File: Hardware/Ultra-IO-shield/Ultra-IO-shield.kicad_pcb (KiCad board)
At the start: 4 copper layers, 158.3 x 36.7 mm, 89 parts, among them J1 Conn_01x04, J10 ASSMANN_A-DF_09_PP/Z, J11 TC_1578891_SCART, J12 Conn_01x01, J13 Conn_01x02, J14 CUI_SD-50BV, J15 Conn_01x02, J16 CUI_SD-50BV, J17 CUI_SD-50BV, J18 Conn_01x04, J19 Conn_01x04, J2 DIN-8_SD-80BV, J20 Conn_01x02, J21 ASSMANN_A-DF_09_PP/Z, J22 Conn_01x02, J3 Conn_01x04, J4 Conn_01x06, J5 Conn_01x02, J6 Conn_RCJ-023, J7 Conn_RCJ-022, J8 Conn_01x02, J9 NorComp_111-014-213L001, Q1 MMBT2907AM3T5G, U1 LM211, U2 AP7370, U3 ADuM226

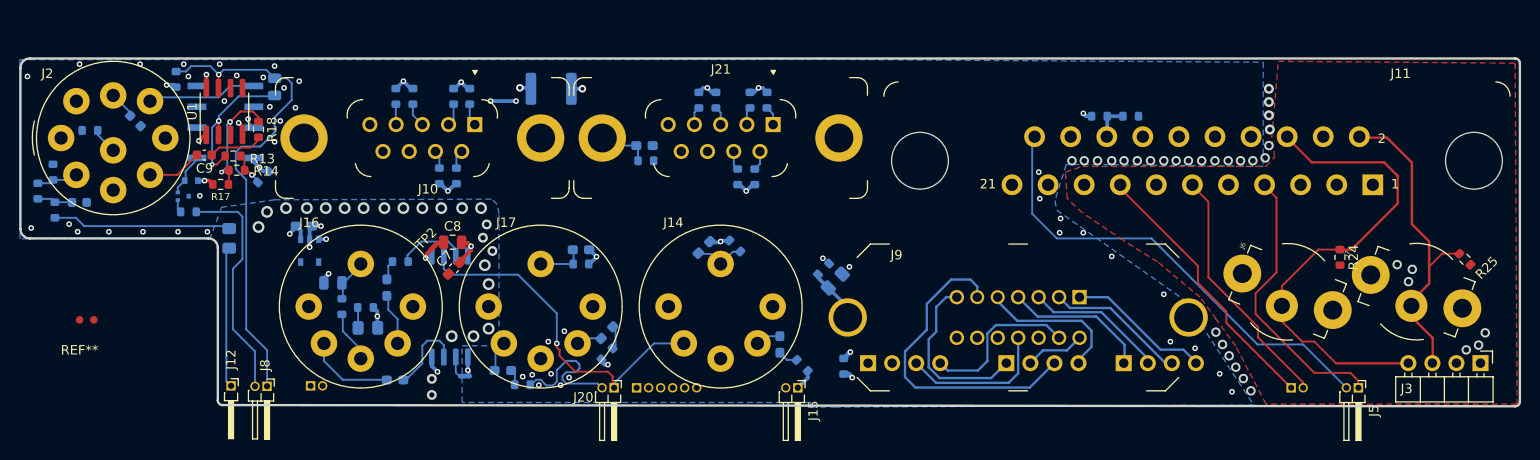
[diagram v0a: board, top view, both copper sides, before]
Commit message: Redesigning of the IO-shield, to make room for Keyboard, power and USB.
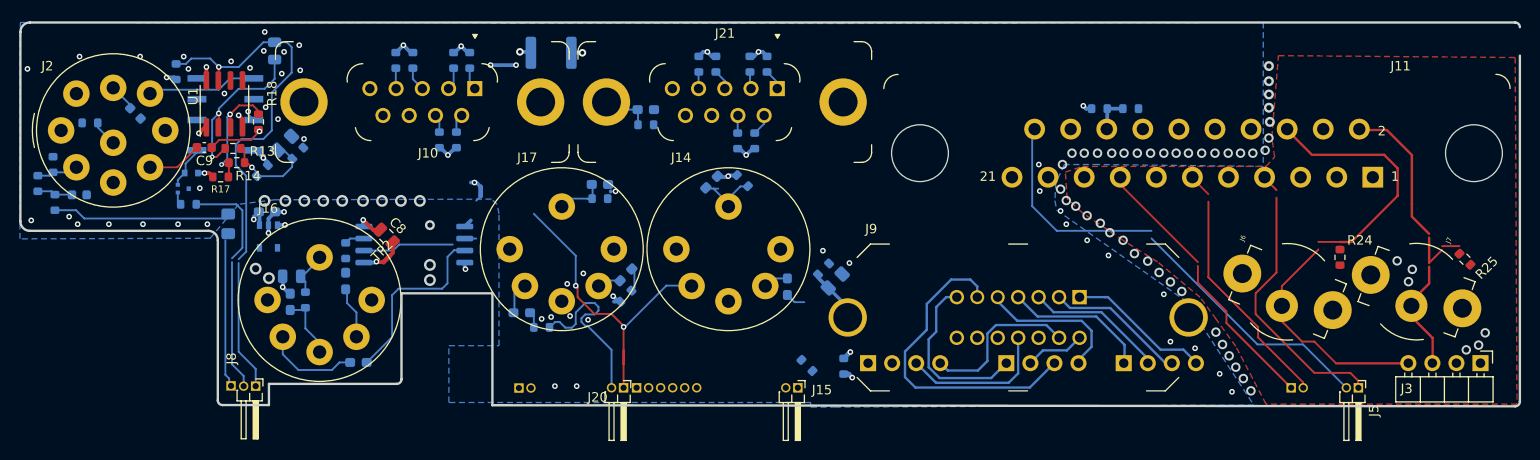
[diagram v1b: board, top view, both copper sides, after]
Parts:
- removed REF**: TestPoint_Bridge_Pitch1.5mm_Pad0.8mm, LRJ:TestPoint_Bridge_Pitch1.5mm_Pad0.8mm
- C7, J12: moved to B.Cu
- moved J13 22.0 mm to (143.0, 109.5)
- moved C2 21.4 mm to (118.3, 83.7), turned to 45 degrees
- moved TP1 19.6 mm to (139.0, 88.8), turned to -90 degrees
- moved R16 17.8 mm to (119.7, 84.7), turned to 45 degrees
- moved C7 17.7 mm to (118.8, 100.4), turned to 90 degrees
- moved U3 7.55 mm to (132.0, 94.3), turned to 0 degrees
- moved C3 7.18 mm to (151.6, 88.0)
- moved R6 7.18 mm to (151.6, 89.5)
- moved C8 7.03 mm to (129.0, 93.5), turned to 135 degrees
- moved C1 6.95 mm to (163.3, 87.8)
- moved R2 6.95 mm to (166.6, 87.6)
- moved J17 6.46 mm to (147.5, 94.8)
- moved FB1 6.42 mm to (154.3, 97.5)
- moved FB5 6.42 mm to (143.3, 101.5)
- moved R5 6.42 mm to (154.3, 99.8)
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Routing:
- net +12V: track 86.8 -> 45.4 mm
- net /CSINKi: track 8.58 -> 19.5 mm
- net /MID_RX: track 37.1 -> 43.6 mm, vias 1 -> 2
- net /CSRCi: track 7.66 -> 2.12 mm
- net Net-(C2-Pad1): track 5.85 -> 10.7 mm
- net GND: track 11.0 -> 6.58 mm
- net /CAS_IN: track 52.0 -> 56.3 mm
- net /MID_TX: track 15.3 -> 19.1 mm
- net +5V: track 27.7 -> 24.2 mm
- net Net-(R12-Pad1): track 15.4 -> 17.9 mm
- net Net-(FB2-Pad2): track 1.88 -> 0.00 mm
- net /+12V-1K: track 74.8 -> 76.7 mm
- net Net-(C7-Pad1): track 5.33 -> 6.99 mm
- net /+5VD_: track 13.9 -> 15.2 mm
- net /CAS_OUT: track 14.9 -> 16.0 mm
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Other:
- board size 158.3 x 36.7 mm -> 158.3 x 40.5 mm

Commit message: Multiple redesigns of the IO-shield. Replaced FPGA with lower pin-count AT10K, since the higher pin-count one is now obsolete.
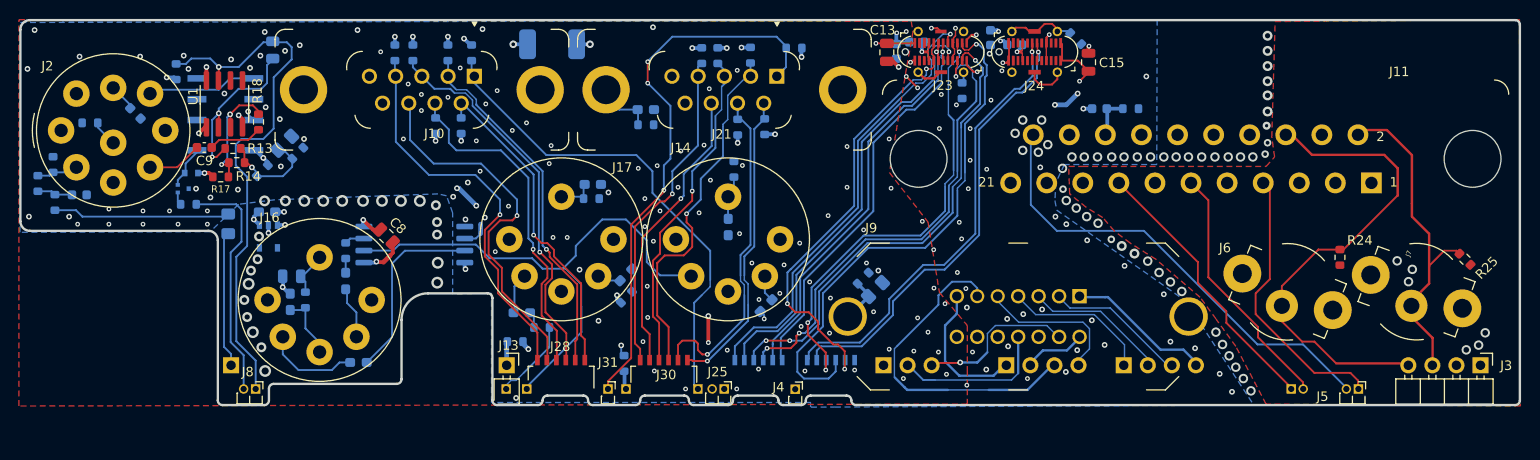
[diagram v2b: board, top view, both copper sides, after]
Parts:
- added C13: C_GRM21BR61A476ME15K, Capacitor_SMD:C_0805_2012Metric, F.Cu at (181.8, 74.0)
- added C14: C_CL10B104KB8NNNL, LRJ:C_0603_1608Metric_round_court, B.Cu at (182.8, 74.0)
- added C15: C_GRM21BR61A476ME15K, Capacitor_SMD:C_0805_2012Metric, F.Cu at (203.2, 75.1)
- added C16: C_CL10B104KB8NNNL, LRJ:C_0603_1608Metric_round_court, B.Cu at (192.8, 72.5)
- added F2: PPTC_0603L075, Fuse:Fuse_0603_1608Metric, B.Cu at (185.0, 73.0)
- added F3: PPTC_0603L075, Fuse:Fuse_0603_1608Metric, B.Cu at (195.3, 73.2)
- added J23: USB_C_GCT_USB4115-03-C, LRJ:USB_C_Receptacle_GCT_USB4115-03-C, F.Cu at (187.6, 74.0)
- added J24: USB_C_GCT_USB4115-03-C, LRJ:USB_C_Receptacle_GCT_USB4115-03-C, F.Cu at (197.5, 74.0)
- added J25: Conn_01x02, LRJ:PinHeader_1x02_P1.27mm_Horizontal_less-silk, F.Cu at (164.7, 109.6)
- added J26: BC075-06, LRJ:GCT_BC075-06_PinHeader_1x06_P1.00mm_Horizontal_SMD, B.Cu at (168.3, 107.3)
- added J27: BC075-06, LRJ:GCT_BC075-06_PinHeader_1x06_P1.00mm_Horizontal_SMD, B.Cu at (175.9, 107.3)
- added J28: BC075-06, LRJ:GCT_BC075-06_PinHeader_1x06_P1.00mm_Horizontal_SMD, F.Cu at (147.4, 107.3)
- added J29: Conn_01x02, LRJ:PinHeader_1x01_P1.27mm_Horizontal_less-silk, B.Cu at (161.9, 109.6)
- added J30: BC075-06, LRJ:GCT_BC075-06_PinHeader_1x06_P1.00mm_Horizontal_SMD, F.Cu at (158.3, 107.3)
- added J31: Conn_01x02, LRJ:PinHeader_1x01_P1.27mm_Horizontal_less-silk, F.Cu at (152.4, 109.6)
- added J32: Conn_01x02, LRJ:PinHeader_1x01_P1.27mm_Horizontal_less-silk, B.Cu at (143.8, 109.6)
- added R39: R_ERJ-3GEYJ105V, Resistor_SMD:R_0603_1608Metric, B.Cu at (189.8, 78.1)
- added R40: R_ERJ-3GEYJ105V, Resistor_SMD:R_0603_1608Metric, B.Cu at (201.8, 72.6)
- C11, C9: value C -> 22nF
- F1: footprint Fuse:Fuse_1812_4532Metric -> LRJ:Yageo_Fuse_1812_4532Metric
- J12: footprint Connector_PinHeader_1.27mm:PinHeader_1x01_P1.27mm_Horizontal -> LRJ:PinHeader_1x01_P2.54mm_Horizontal_less-silk
- J13: value Conn_01x02 -> Conn_01x01; footprint Connector_PinHeader_1.27mm:PinHeader_1x02_P1.27mm_Horizontal -> LRJ:PinHeader_1x01_P2.54mm_Horizontal_less-silk; moved to F.Cu
- J15, J20: footprint Connector_PinHeader_1.27mm:PinHeader_1x02_P1.27mm_Horizontal -> LRJ:PinHeader_1x01_P1.27mm_Horizontal_less-silk; moved to B.Cu
- J19: value Conn_01x04 -> Conn_01x03; footprint LRJ:PinHeader_1x04_P2.54mm_Horizontal_less-silk -> LRJ:PinHeader_1x03_P2.54mm_Horizontal_less-silk
- J22, J5, J8: footprint Connector_PinHeader_1.27mm:PinHeader_1x02_P1.27mm_Horizontal -> LRJ:PinHeader_1x02_P1.27mm_Horizontal_less-silk
- J4: value Conn_01x06 -> Conn_01x02; footprint Connector_PinHeader_1.27mm:PinHeader_1x06_P1.27mm_Horizontal -> LRJ:PinHeader_1x01_P1.27mm_Horizontal_less-silk; moved to F.Cu
- R11, R23: value R -> 1K
- R12: value R -> 220K; footprint Resistor_SMD:R_0805_2012Metric -> LRJ:R_0805_2012Metric_roundcourt
- R13, R21, R22: value R -> 4.7K
- R14, R18: value R -> 10K
- R15, R16: value R -> 2.7K
- R17: value R -> 470K
- R20: value R -> 100R
- R8: footprint Resistor_SMD:R_0603_1608Metric -> LRJ:C_0603_1608Metric_round_court
- TP1, TP2: value TestPoint_2Pole -> NetTie-2_small_round
- U3: footprint Package_SO:SOIC-8_7.5x5.85mm_P1.27mm -> LRJ:TEXAS_RI-8-1_7.5x5.85mm_P1.27mm
- moved R10 34.8 mm to (142.6, 104.6), turned to 180 degrees
- moved R1 19.3 mm to (154.1, 106.9), turned to 90 degrees
- moved J15 18.2 mm to (154.3, 109.6)
- moved J4 16.8 mm to (172.2, 109.6)
- moved J20 12.4 mm to (141.7, 109.6)
- moved C1 5.06 mm to (165.1, 92.5), turned to -90 degrees
- moved C100 4.34 mm to (180.7, 99.1)
- moved R100 4.29 mm to (179.3, 97.9)
- moved TP1 3.95 mm to (139.0, 92.7)
- moved R30 3.32 mm to (172.1, 73.6), turned to 0 degrees
- moved FB4 3.01 mm to (169.1, 100.8), turned to -135 degrees
- moved J13 2.73 mm to (141.7, 107.1)
- moved J12 2.18 mm to (112.6, 107.1)
- moved R36 1.83 mm to (168.9, 81.9)
- moved J19 1.65 mm to (181.5, 107.1)
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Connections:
- J19 pad 1: +12V -> +5V
- J19 pad 2: +5V -> /PRT_BUSY
- J19 pad 3: /PRT_BUSY -> /PD7
- J20 pad 1: /MID_RX -> /MID_TX
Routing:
- net /~{FWD_B}: track 2.20 -> 58.0 mm, vias 0 -> 3
- net /RX2+: track 0.00 -> 55.2 mm, vias 0 -> 1
- net /GND_U: track 0.00 -> 52.6 mm, vias 0 -> 8
- net /RX1+: track 0.00 -> 50.1 mm, vias 0 -> 3
- net /RX1-: track 0.00 -> 50.0 mm, vias 0 -> 3
- net /~{FWD_A}: track 2.38 -> 51.6 mm
- net /USB2_D+: track 0.00 -> 48.5 mm, vias 0 -> 1
- net /USB2_D-: track 0.00 -> 48.4 mm, vias 0 -> 1
- net /SBU1/AUX1+: track 0.00 -> 47.5 mm, vias 0 -> 1
- net /RX2-: track 0.00 -> 47.1 mm, vias 0 -> 3
- net /SBU2/AUX1-: track 0.00 -> 46.5 mm, vias 0 -> 1
- net /CC1/HPD: track 0.00 -> 46.4 mm, vias 0 -> 3
- net /USB1_D-: track 0.00 -> 42.4 mm, vias 0 -> 1
- net /USB1_D+: track 0.00 -> 42.3 mm, vias 0 -> 1
- net /~{RGT_A}: track 2.17 -> 42.1 mm, vias 0 -> 1
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- added copper zone on F.Cu, net GND
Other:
- board size 158.3 x 40.5 mm -> 158.3 x 40.6 mm

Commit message: Added cooler and CPU-mount footprints, as well as Indication LEDs.
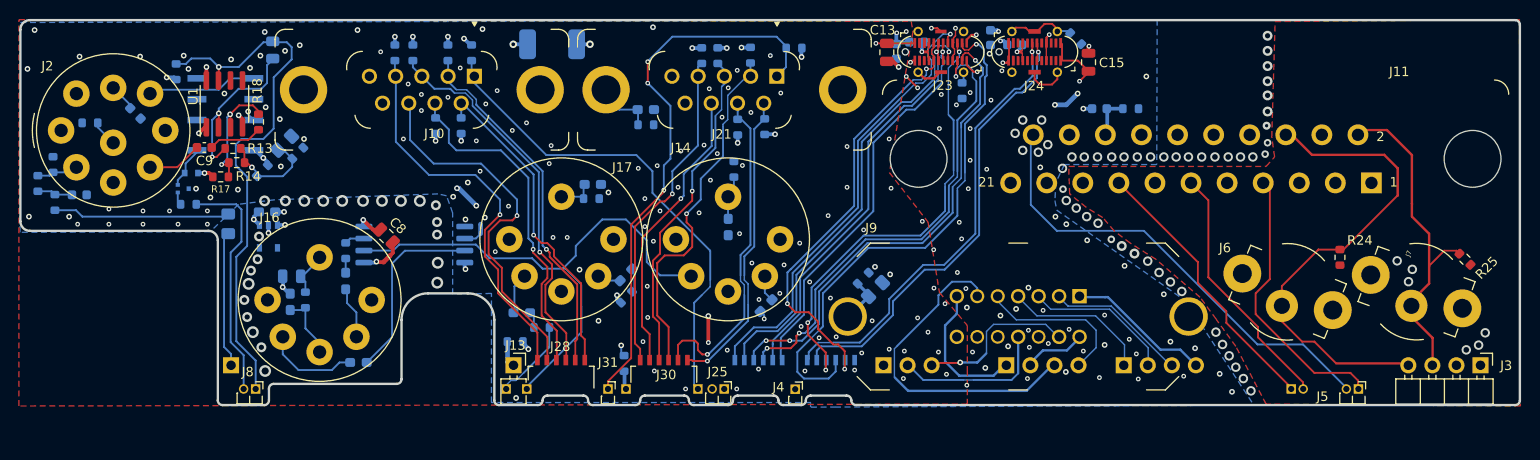
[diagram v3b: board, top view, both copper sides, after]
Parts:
- moved J13 0.73 mm to (142.4, 107.1)
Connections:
- net /RX1+ renamed /SWDIO/RX1+
- net /RX1- renamed /SWDCLK/RX1-
- net /RX2+ renamed /nRESET/RX2+
- net /RX2- renamed /SWO/RX2-
- net /SBU1/AUX1+ renamed /VCT/SBU1
- net /SBU2/AUX1- renamed /GND/SBU2
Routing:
- net /PD3: track 15.4 -> 16.6 mm
- net /PD1: track 14.7 -> 15.4 mm
- net GND: vias 158 -> 177
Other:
- outline, holes or cut-outs redrawn

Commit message: Started fixing many small issues.
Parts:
- removed TP2: NetTie-2_small_round, NetTie:NetTie-2_SMD_Pad0.5mm
- added C17: C_CL10B104KB8NNNL, Capacitor_SMD:C_0603_1608Metric_Pad1.08x0.95mm_HandSolder, B.Cu at (201.1, 80.0)
- added J33: Conn_01x02, LRJ:PinHeader_1x01_P1.27mm_Horizontal_less-silk, F.Cu at (217.1, 109.6)
- added R41: R_ERJ-3GEYJ105V, Resistor_SMD:R_0603_1608Metric, B.Cu at (194.9, 90.8)
- J23, J24: footprint LRJ:USB_C_Receptacle_GCT_USB4115-03-C -> LRJ:GCT_USB4115-03-C_modified
- J26, J27, J28, J30: footprint LRJ:GCT_BC075-06_PinHeader_1x06_P1.00mm_Horizontal_SMD -> LRJ:GCT_BC075-06_PinHeader_1x06_P1.00mm_Horizontal_SMD_less-silk
- moved R100 33.1 mm to (212.4, 98.8)
- moved C100 7.70 mm to (186.5, 104.1), turned to 180 degrees
- moved J21 5.74 mm to (164.7, 78.0)
- moved J10 5.72 mm to (132.8, 78.0)
- moved F2 0.72 mm to (184.3, 72.8), turned to 135 degrees
- moved J1 0.67 mm to (206.2, 107.1)
- moved C14 0.65 mm to (182.2, 73.7)
- moved R27 0.50 mm to (135.0, 74.1)
- moved R23 0.05 mm to (108.1, 90.2)
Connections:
- net /2.5V renamed /BLANK
- net Earth renamed GND2
- net Net-(J23-PadSH) renamed /SH1
- net Net-(J24-PadSH) renamed /SH2
- C100 pad 1: Net-(C100-Pad1) -> Net-(J9-Pin_14)
- C8 pad 1: +5VD -> /+5VD
- J11 pad 13: GNDA -> GND
- J11 pad 17: GNDA -> GND
- J11 pad 21: GND -> /SH3
- J11 pad 4: GNDA -> GND
- J11 pad 5: GNDA -> GND
- J11 pad 9: GNDA -> GND
- J3 pad 1: GNDA -> GND
- J3 pad 2: GNDA -> GND
- J6 pad 1A: GNDA -> GND
- J6 pad 1B: GNDA -> GND
- J7 pad 1A: GNDA -> GND
- J7 pad 1B: GNDA -> GND
- J9 pad 14: GND -> Net-(J9-Pin_14)
- J9 pad 15: Net-(C100-Pad1) -> Net-(J9-SH)
- J9 pad 16: unconnected-(J9-Pad16) -> Net-(J9-SH)
- R100 pad 2: Net-(C100-Pad1) -> Net-(J9-SH)
- R24 pad 2: GNDA -> GND
- R25 pad 1: GNDA -> GND
- U2 pad 3: /+5VD_ -> /+5VD
- U3 pad 1: /+5VD_ -> /+5VD
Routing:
- net /BLANK: track 3.86 -> 56.9 mm
- net Net-(J9-SH): track 0.00 -> 44.1 mm, vias 0 -> 2
- net /+5VD: track 0.00 -> 17.2 mm, vias 0 -> 2
- net /+5VD_: track 15.2 -> 0.00 mm, vias 2 -> 0
- net Net-(C100-Pad1): track 4.95 -> 0.00 mm
- net /SH2: track 22.3 -> 19.9 mm
- net /CSYNC: track 48.8 -> 46.6 mm
- net /SH3: track 0.00 -> 2.10 mm
- net Net-(J9-Pin_14): track 0.00 -> 1.70 mm
- net +5VD: track 1.49 -> 0.00 mm
- net Net-(C12-Pad1): track 75.7 -> 77.1 mm, vias 0 -> 3
- net /PD5: track 15.0 -> 16.0 mm
- net GND: track 4.77 -> 5.62 mm, vias 177 -> 205
- net /~{TRG2_B}: track 34.7 -> 35.5 mm
- net /~{STROBE}: track 15.3 -> 14.6 mm
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- removed copper zone on F.Cu, net GNDA
- removed copper zone on In1.Cu, net GNDA
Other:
- outline, holes or cut-outs redrawn
